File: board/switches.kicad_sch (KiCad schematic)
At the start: 37 parts, among them Q2 IPB180N10S4-02, Q3 Si4162DY, Q5 Si4162DY, Q6 Si4162DY, Q7 Si4162DY, Q8 Si4162DY, U1 LT1910, U11 LT1910, U12 LT1910, U13 LT1910, U14 LT1910, U19 LT1910

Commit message: 17 hours of our lives
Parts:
- TP4: footprint Connector_Pin:Pin_D1.1mm_L10.2mm_W3.5mm_Flat -> TestPoint:TestPoint_Pad_D1.0mm
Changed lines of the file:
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@@
+	)
+	(symbol
+		(lib_id "Connector:TestPoint")
+		(at 72.39 64.77 90)
+		(unit 1)
+		(exclude_from_sim no)
+		(in_bom yes)
+		(on_board yes)
+		(dnp no)
+		(fields_autoplaced yes)
+		(property "Reference" "TP4"
+			(at 69.088 59.69 90)
+			(effects
+				(font
+					(size 1.27 1.27)
+				)
+			)
+		)
+		(property "Value" "TestPoint"
+			(at 69.088 62.23 90)
+			(effects
+				(font
+					(size 1.27 1.27)
+				)
+			)
+		)
+		(property "Footprint" "TestPoint:TestPoint_Pad_D1.0mm"
+			(at 72.39 59.69 0)
+			(effects
+				(font
+					(size 1.27 1.27)
+				)
+				(hide yes)
+			)
+		)
+		(property "Datasheet" "~"
+			(at 72.39 59.69 0)
+			(effects
+				(font
+					(size 1.27 1.27)
+				)
+				(hide yes)
+			)
+		)
+		(property "Description" "test point"
+			(at 72.39 64.77 0)
+			(effects
+				(font
+					(size 1.27 1.27)
+				)
+				(hide yes)
+			)
+		)
+		(pin "1"
+		)
+		(instances
+			(project "PowerManagementBoard"
+				(path "/7eaa639d-7062-45e7-be05-1c2855431307/d051b168-830a-4a55-b5cd-142fa18015a1"
+					(reference "TP4")
+					(unit 1)
+				)
+			)
+		)
 	)
 	(symbol
@@
 					(unit 1)
 				)
-			)
-		)
-	)
-	(symbol
-		(lib_id "Connector:TestPoint")
-		(at 72.39 64.77 90)
-		(unit 1)
-		(exclude_from_sim no)
-		(in_bom yes)
-		(on_board yes)
-		(dnp no)
-		(fields_autoplaced yes)
-		(property "Reference" "TP4"
-			(at 69.088 59.69 90)
-			(effects
-				(font
-					(size 1.27 1.27)
-				)
-			)
-		)
-		(property "Value" "TestPoint"
-			(at 69.088 62.23 90)
-			(effects
-				(font
-					(size 1.27 1.27)
-				)
-			)
-		)
-		(property "Footprint" "Connector_Pin:Pin_D1.1mm_L10.2mm_W3.5mm_Flat"
-			(at 72.39 59.69 0)
-			(effects
-				(font
-					(size 1.27 1.27)
-				)
-				(hide yes)
-			)
-		)
-		(property "Datasheet" "~"
-			(at 72.39 59.69 0)
-			(effects
-				(font
-					(size 1.27 1.27)
-				)
-				(hide yes)
-			)
-		)
-		(property "Description" "test point"
-			(at 72.39 64.77 0)
-			(effects
-				(font
-					(size 1.27 1.27)
-				)
-				(hide yes)
-			)
-		)
-		(pin "1"
-		)
-		(instances
-			(project "PowerManagementBoard"
-				(path "/7eaa639d-7062-45e7-be05-1c2855431307/d051b168-830a-4a55-b5cd-142fa18015a1"
-					(reference "TP4")
-					(unit 1)
-				)

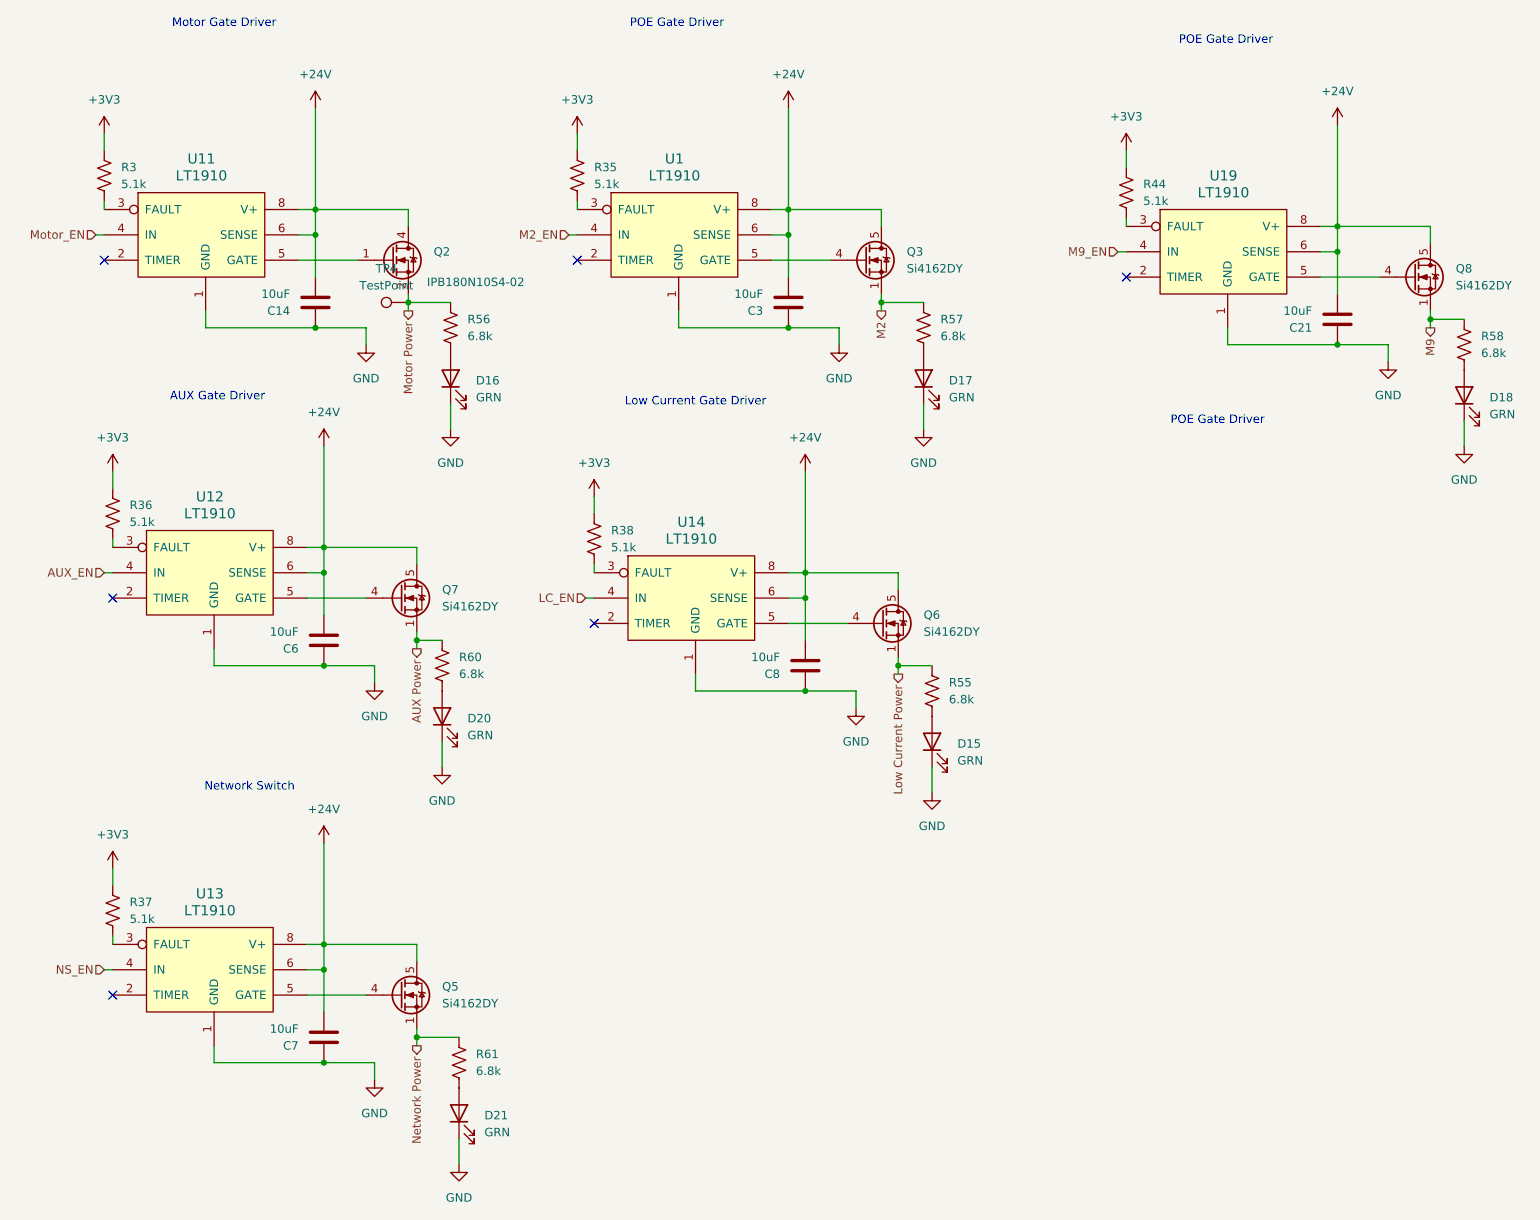
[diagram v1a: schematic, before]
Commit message: Center schematics and layout for prettiness
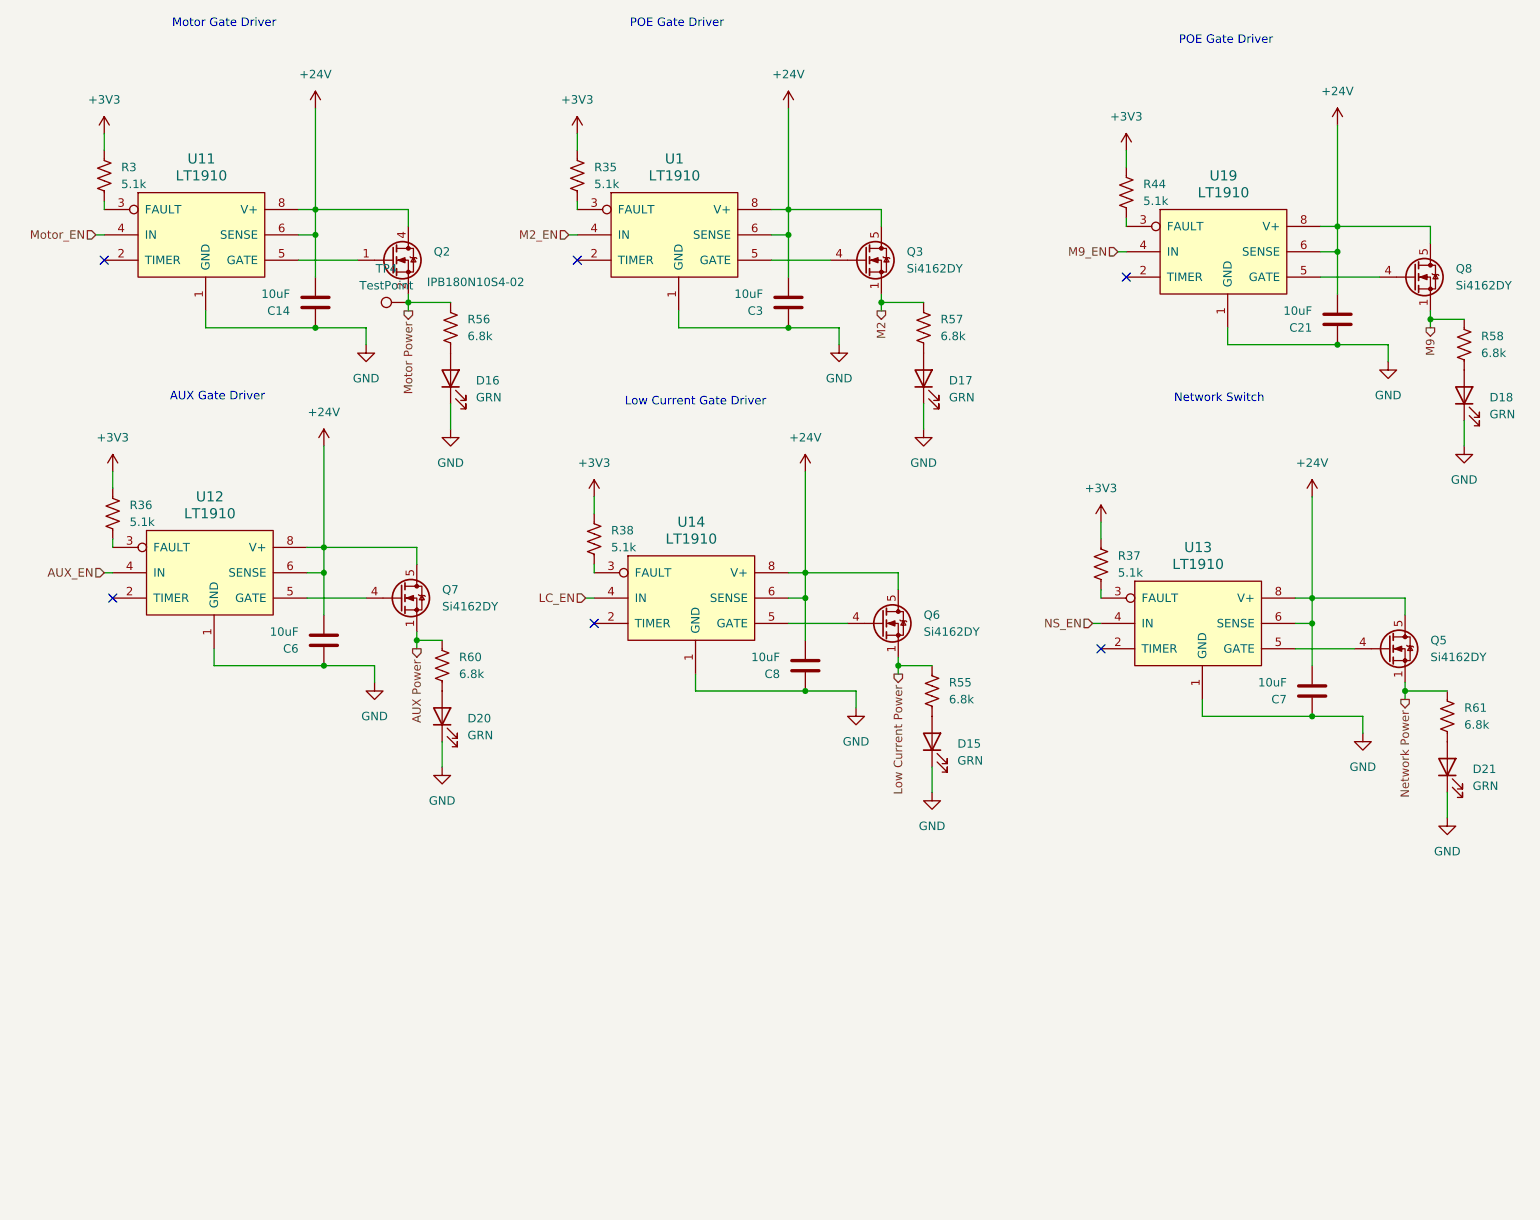
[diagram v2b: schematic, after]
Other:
- moved on the sheet: C7, D21, Q5, R37, R61, U13

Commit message: add label for battery sensing molex connector
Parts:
- renumbered C6 to C10, C7 to C14, C21 to C15, C3 to C16, C14 to C8, C8 to C9, D21 to D11, D18 to D12, D17 to D13, D16 to D2, D15 to D3, D20 to D4, Q6 to Q2, Q7 to Q3, Q2 to Q4, Q8 to Q6, Q3 to Q7, R55 to R2, R60 to R3, R37 to R30, R61 to R31, R44 to R32, R58 to R33, R35 to R34, R57 to R35, R56 to R4, R3 to R5, R38 to R7, R36 to R8, TP4 to TP1, U19 to U10, U1 to U11, U11 to U2, U14 to U3, U12 to U4, U13 to U9
